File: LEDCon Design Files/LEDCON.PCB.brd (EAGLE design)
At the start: 81.7 x 51.7 mm, 29 parts

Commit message: LEDCON.PCB.v1.0
Everything done. Release version.
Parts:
- U$5: device KW2:RGBLED -> KW2:PLCC4_SMALL
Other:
- board text added: "R.S 2/20/15"
- board text removed: "R.S 2/19/15"
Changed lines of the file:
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@@
 <setting verticaltext="up"/>
 </settings>
-<grid distance="0.1" unitdist="mm" unit="mm" style="lines" multiple="1" display="yes" altdistance="0.000000123031" altunitdist="inch" altunit="inch"/>
+<grid distance="0.0999999999" unitdist="mm" unit="mm" style="lines" multiple="1" display="yes" altdistance="0.000000123031" altunitdist="inch" altunit="inch"/>
 <layers>
 <layer number="1" name="Top" color="4" fill="1" visible="yes" active="yes"/>
@@
 <rectangle x1="2.136709375" y1="19.902615625" x2="2.741228125" y2="19.920396875" layer="21" rot="R180"/>
 <rectangle x1="2.243390625" y1="19.920396875" x2="2.598990625" y2="19.938171875" layer="21" rot="R180"/>
-<text x="-16.26518125" y="20.362359375" size="1.016" layer="21" font="vector" ratio="15" rot="SR0">R.S 2/19/15</text>
+<text x="-16.26518125" y="20.362359375" size="1.016" layer="21" font="vector" ratio="15" rot="SR0">R.S 2/20/15</text>
 </plain>
 <attributes>
@@
 <param name="mdDrill" value="0.25mm"/>
 <param name="mdSmdStop" value="0mil"/>
-<param name="msWidth" value="10mil"/>
-<param name="msDrill" value="24mil"/>
+<param name="msWidth" value="2.75mil"/>
+<param name="msDrill" value="6mil"/>
 <param name="msMicroVia" value="9.99mm"/>
 <param name="msBlindViaRatio" value="0.5"/>
@@
 <param name="rvMicroViaOuter" value="0.25"/>
 <param name="rvMicroViaInner" value="0.25"/>
-<param name="rlMinPadTop" value="1mil"/>
+<param name="rlMinPadTop" value="6mil"/>
 <param name="rlMaxPadTop" value="20mil"/>
 <param name="rlMinPadInner" value="10mil"/>
 <param name="rlMaxPadInner" value="20mil"/>
-<param name="rlMinPadBottom" value="2mil"/>
+<param name="rlMinPadBottom" value="6mil"/>
 <param name="rlMaxPadBottom" value="20mil"/>
 <param name="rlMinViaOuter" value="8mil"/>
@@
 </autorouter>
 <elements>
-<element name="U$1" library="KW2" package="MATE-N-LOK_643230-1" value="" x="3.9116" y="-14.1224" locked="yes" rot="MR180">
+<element name="U$1" library="KW2" package="MATE-N-LOK_643230-1" value="" x="3.9116" y="-14.1224" locked="yes" smashed="yes" rot="MR180">
 <attribute name="MFGN" value="TE Connectivity" x="3.9116" y="-14.1224" size="1.778" layer="28" rot="MR180" display="off"/>
 <attribute name="MFGP" value="643230-1" x="3.9116" y="-14.1224" size="1.778" layer="28" rot="MR180" display="off"/>
+<attribute name="NAME" x="11.9916" y="-10.4724" size="1.27" layer="22" rot="MR180"/>
 </element>
 <element name="U$2" library="GW-devices" package="ESWITCH-TL3301PF" value="" x="-35" y="0" locked="yes" smashed="yes" rot="R90">
@@
 <attribute name="MFGN" value="CUI" x="31.75" y="16.3322" size="1.778" layer="28" rot="MR90" display="off"/>
 <attribute name="MFGP" value="PJ-002A" x="31.75" y="16.3322" size="1.778" layer="28" rot="MR90" display="off"/>
-<attribute name="NAME" x="26.37" y="17.8478" size="1.27" layer="22" rot="MR270"/>
+<attribute name="NAME" x="26.37" y="17.8478" size="1.016" layer="22" rot="MR270"/>
 </element>
 <element name="U$4" library="KW2" package="DF12_F" value="" x="-23.57" y="10" locked="yes" smashed="yes" rot="MR270">
 <attribute name="MFGN" value="Hirose" x="-23.57" y="10" size="1.778" layer="28" rot="MR270" display="off"/>
 <attribute name="MFGP" value="DF12(3.0)-40DP-0.5V(86)" x="-23.57" y="10" size="1.778" layer="28" rot="MR270" display="off"/>
-<attribute name="NAME" x="-28.55" y="11.94" size="1.27" layer="22" rot="MR270"/>
+<attribute name="NAME" x="-28.55" y="11.94" size="1.016" layer="22" rot="MR270"/>
 </element>
 <element name="U$6" library="texas" package="PW_R-PDSO-G14" value="" x="1.4026" y="3.5886" smashed="yes" rot="R270">
@@
 <attribute name="MFGN" value="WorldSemi" x="19.71" y="-2.4" size="1.778" layer="28" rot="MR90" display="off"/>
 <attribute name="MFGP" value="WS2801" x="19.71" y="-2.4" size="1.778" layer="28" rot="MR90" display="off"/>
-<attribute name="NAME" x="18.405" y="-7.58" size="1.27" layer="22" rot="MR180"/>
+<attribute name="NAME" x="18.905" y="-7.58" size="1.016" layer="22" rot="MR180"/>
 <attribute name="VALUE" x="19.075" y="-6.21" size="1.27" layer="28" rot="MR90"/>
 </element>
@@
 <attribute name="MFGN" value="Vishay Dale" x="12.32" y="1.14" size="1.778" layer="28" rot="MR0" display="off"/>
 <attribute name="MFGP" value="CRCW080524R0FKEA" x="12.32" y="1.14" size="1.778" layer="28" rot="MR0" display="off"/>
-<attribute name="NAME" x="10.22" y="0.64" size="1.27" layer="22" rot="MR0"/>
+<attribute name="NAME" x="9.92" y="0.54" size="1.016" layer="22" rot="MR0"/>
 </element>
 <element name="U$16" library="GW-devices" package="RF-C0805" value="24Ohm" x="12.31" y="-1.4" smashed="yes" rot="MR0">
-<attribute name="NAME" x="9.91" y="-2" size="1.27" layer="22" rot="MR0"/>
+<attribute name="NAME" x="9.91" y="-1.8" size="1.016" layer="22" rot="MR0"/>
 <attribute name="MFGN" value="Vishay Dale" x="12.31" y="-1.4" size="1.778" layer="28" rot="MR0" display="off"/>
 <attribute name="MFGP" value="CRCW080524R0FKEA" x="12.31" y="-1.4" size="1.778" layer="28" rot="MR0" display="off"/>
 </element>
 <element name="U$17" library="GW-devices" package="RF-C0805" value="24Ohm" x="12.31" y="-3.64" smashed="yes" rot="MR0">
-<attribute name="NAME" x="9.81" y="-4.34" size="1.27" layer="22" rot="MR0"/>
+<attribute name="NAME" x="10.01" y="-4.14" size="1.016" layer="22" rot="MR0"/>
 <attribute name="MFGN" value="Vishay Dale" x="12.31" y="-3.64" size="1.778" layer="28" rot="MR0" display="off"/>
 <attribute name="MFGP" value="CRCW080524R0FKEA" x="12.31" y="-3.64" size="1.778" layer="28" rot="MR0" display="off"/>
@@
 <attribute name="MFGN" value="CNC Tech" x="-0.635" y="-8.225" size="1.778" layer="28" rot="MR0" display="off"/>
 <attribute name="MFGP" value="3220-20-0100-00" x="-0.635" y="-8.225" size="1.778" layer="28" rot="MR0" display="off"/>
-<attribute name="NAME" x="0.975" y="-13.305" size="1.27" layer="22" rot="MR0"/>
+<attribute name="NAME" x="1.875" y="-12.805" size="1.016" layer="22" rot="MR0"/>
 </element>
 <element name="U$20" library="GW-devices" package="RF-C0805" value="68k" x="11" y="-0.6" smashed="yes" rot="R270">
 <attribute name="MFGN" value="Vishay Dale" x="11" y="-0.6" size="1.778" layer="27" rot="R270" display="off"/>
 <attribute name="MFGP" value="CRCW080568K0FKEA" x="11" y="-0.6" size="1.778" layer="27" rot="R270" display="off"/>
-<attribute name="NAME" x="8.3" y="1.2" size="1.016" layer="21" rot="R270"/>
+<attribute name="NAME" x="8.3" y="0.8" size="1.016" layer="21" rot="R270"/>
 </element>
 <element name="U$21" library="GW-devices" package="RF-C0805" value="68k" x="10.1" y="3.7" smashed="yes" rot="R90">
-<attribute name="NAME" x="7.5" y="5.8" size="1.016" layer="21" rot="R270"/>
+<attribute name="NAME" x="7.8" y="5.5" size="1.016" layer="21" rot="R270"/>
 <attribute name="MFGN" value="Vishay Dale" x="10.1" y="3.7" size="1.778" layer="27" rot="R90" display="off"/>
 <attribute name="MFGP" value="CRCW080568K0FKEA" x="10.1" y="3.7" size="1.778" layer="27" rot="R90" display="off"/>
@@
 <attribute name="MFGN" value="Vishay Dale" x="-21.8" y="-6.6" size="1.778" layer="28" rot="MR180" display="off"/>
 <attribute name="MFGP" value="CRCW080510K0FKEA" x="-21.8" y="-6.6" size="1.778" layer="28" rot="MR180" display="off"/>
-<attribute name="NAME" x="-23.3" y="-8.4" size="1.27" layer="22" rot="MR180"/>
+<attribute name="NAME" x="-23" y="-8.3" size="1.016" layer="22" rot="MR180"/>
 </element>
 <element name="U$10" library="GW-devices" package="C0805" value="0.1uF" x="27" y="13.1" smashed="yes">
@@
 <attribute name="MFGN" value="OnSemi" x="-18" y="-12.3" size="1.778" layer="27" rot="R180" display="off"/>
 <attribute name="MFGP" value="NCP1117ST33T3G" x="-18" y="-12.3" size="1.778" layer="27" rot="R180" display="off"/>
-<attribute name="NAME" x="-14.0932" y="-10.498" size="1.016" layer="21" rot="R270"/>
+<attribute name="NAME" x="-14.0932" y="-11.298" size="1.016" layer="21" rot="R270"/>
 <attribute name="VALUE" x="-22.8768" y="-8.998" size="1.27" layer="27" rot="R270"/>
 </element>
@@
 <attribute name="NAME" x="-18.83" y="-5.77" size="1.016" layer="21" rot="R180"/>
 </element>
-<element name="U$5" library="KW2" package="RGBLED" value="" x="35" y="0" smashed="yes">
+<element name="U$5" library="KW2" package="PLCC4_SMALL" value="" x="35" y="0" smashed="yes">
 <attribute name="MFGN" value="Cree, Inc." x="35" y="0" size="1.778" layer="27" display="off"/>
 <attribute name="MFGP" value="CLV1A-FKB-CK1N1G1BB7R4S3" x="35" y="0" size="1.778" layer="27" display="off"/>
@@
 </signal>
 </signals>
-<errors>
-</errors>
 </board>
 </drawing>

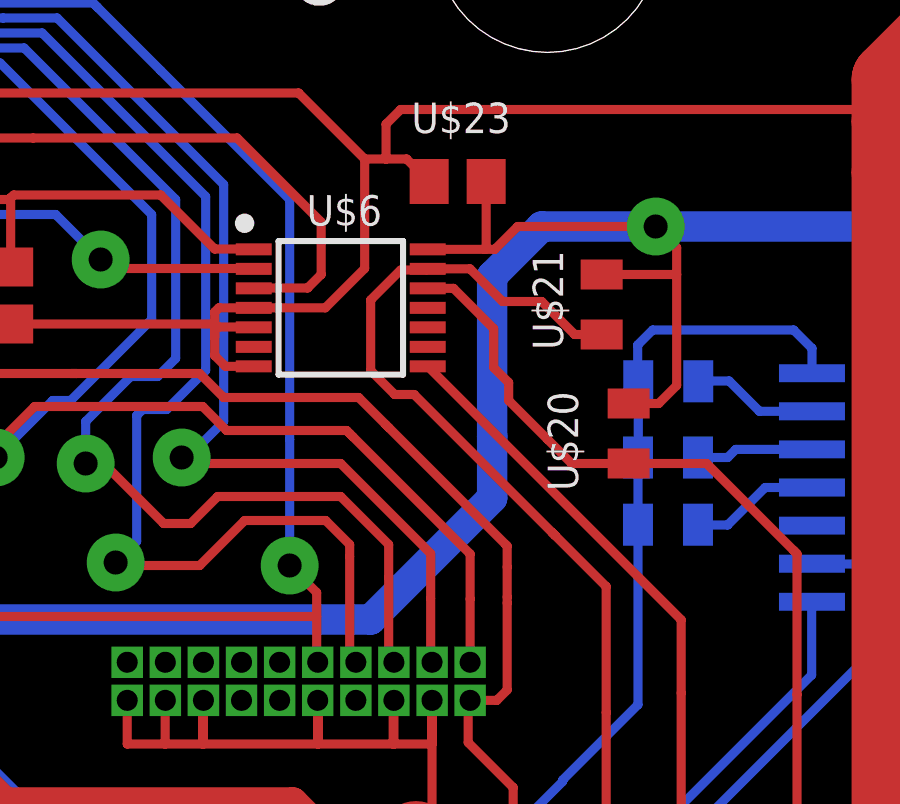
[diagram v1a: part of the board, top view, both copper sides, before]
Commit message: Removed level shifter (no layout change)
Also test commit for branch.
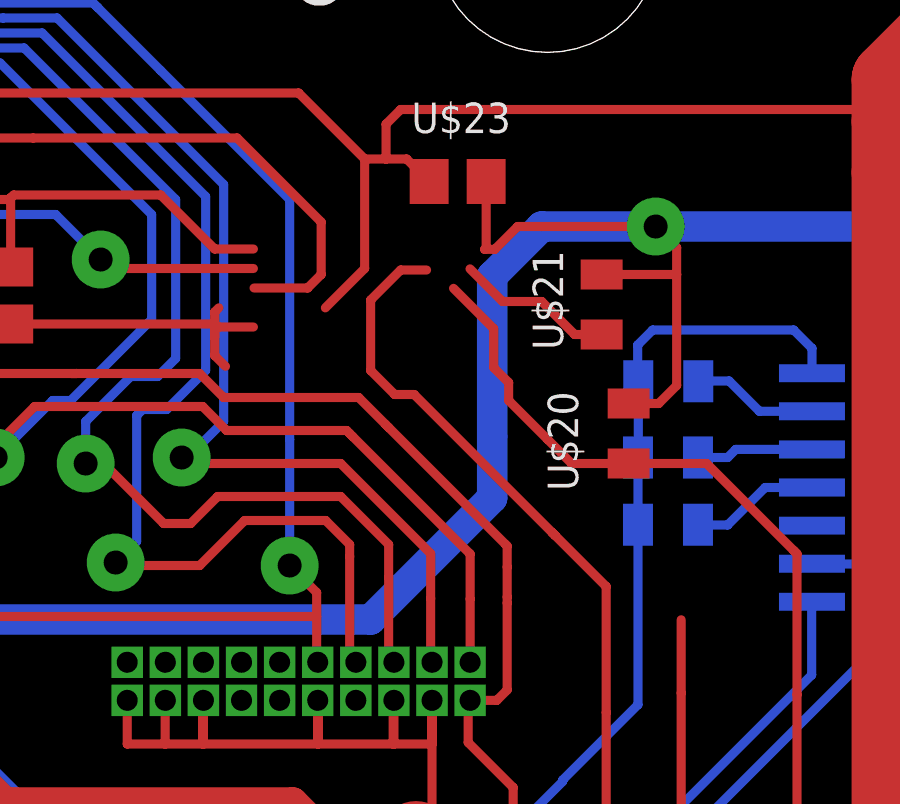
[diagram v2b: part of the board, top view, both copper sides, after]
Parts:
- removed U$6: (no value), texas:PW_R-PDSO-G14
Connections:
- net +3V3: no longer U$6.1, U$6.8
- net CLK_5V: no longer U$6.12
- net DAT_5V: no longer U$6.13
- net GND: no longer U$6.4, U$6.5, U$6.7
- net N$1: no longer U$6.2
- net N$2: no longer U$6.3
- net V+: no longer U$6.14
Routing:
- net +3V3: track 234.5 -> 222.4 mm
- net GND: track 326.4 -> 321.9 mm
- net V+: track 179.3 -> 177.4 mm
- net DAT_5V: track 30.8 -> 29.3 mm
- net CLK_5V: track 26.7 -> 25.9 mm
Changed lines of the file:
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@@
 <?xml version="1.0" encoding="utf-8"?>
 <!DOCTYPE eagle SYSTEM "eagle.dtd">
-<eagle version="6.5.0">
+<eagle version="6.6.0">
 <drawing>
 <settings>
@@
 <attribute name="NAME" x="-28.55" y="11.94" size="1.016" layer="22" rot="MR270"/>
 </element>
-<element name="U$6" library="texas" package="PW_R-PDSO-G14" value="" x="1.4026" y="3.5886" smashed="yes" rot="R270">
-<attribute name="MFGN" value="Texas Instruments" x="1.4026" y="3.5886" size="1.778" layer="27" rot="R270" display="off"/>
-<attribute name="MFGP" value="TXB0104PWR" x="1.4026" y="3.5886" size="1.778" layer="27" rot="R270" display="off"/>
-<attribute name="NAME" x="0.2626" y="6.3286" size="1.016" layer="21"/>
-<attribute name="VALUE" x="-1.1374" y="-0.2214" size="1.27" layer="27"/>
-</element>
 <element name="U$8" library="GW-devices" package="SO14" value="" x="19.71" y="-2.4" smashed="yes" rot="MR90">
 <attribute name="MFGN" value="WorldSemi" x="19.71" y="-2.4" size="1.778" layer="28" rot="MR90" display="off"/>
@@
 <contactref element="U$3" pad="P$2"/>
 <contactref element="U$1" pad="P$1"/>
-<contactref element="U$6" pad="7"/>
-<contactref element="U$6" pad="5"/>
-<contactref element="U$6" pad="4"/>
 <contactref element="U$2" pad="1"/>
 <contactref element="U$2" pad="2"/>
@@
 <wire x1="-21.25" y1="17.25" x2="-21.25" y2="17.1" width="0.3048" layer="16"/>
 <wire x1="-21.25" y1="17.1" x2="-21.25" y2="14.7698" width="0.3048" layer="16"/>
-<wire x1="-1.4974" y1="1.6386" x2="-2.4386" y2="1.6386" width="0.3048" layer="1"/>
 <wire x1="-2.4386" y1="1.6386" x2="-2.8" y2="2" width="0.3048" layer="1"/>
 <wire x1="-2.8" y1="2" x2="-2.8" y2="2.6" width="0.3048" layer="1"/>
 <wire x1="-2.8" y1="2.6" x2="-2.8" y2="2.8" width="0.3048" layer="1"/>
 <wire x1="-2.65" y1="2.95" x2="-1.5088" y2="2.95" width="0.3048" layer="1"/>
-<wire x1="-1.5088" y1="2.95" x2="-1.4974" y2="2.9386" width="0.3048" layer="1"/>
-<wire x1="-1.4974" y1="3.5886" x2="-2.6614" y2="3.5886" width="0.3048" layer="1"/>
 <wire x1="-2.6614" y1="3.5886" x2="-2.8" y2="3.45" width="0.3048" layer="1"/>
 <wire x1="-2.8" y1="3.45" x2="-2.8" y2="3" width="0.3048" layer="1"/>
@@
 <via x="-17.7" y="17.1" extent="1-16" drill="0.8" diameter="1.9304"/>
 <wire x1="-17.7" y1="17.1" x2="-21.25" y2="17.1" width="0.3048" layer="16"/>
-<wire x1="-1.4974" y1="3.5886" x2="0.8886" y2="3.5886" width="0.3048" layer="1"/>
 <wire x1="0.8886" y1="3.5886" x2="2.2" y2="4.9" width="0.3048" layer="1"/>
 <wire x1="2.2" y1="4.9" x2="2.2" y2="8.55" width="0.3048" layer="1"/>
@@
 <wire x1="-34.3" y1="-22.9" x2="-35.3208" y2="-22.9" width="0.3048" layer="16"/>
 <wire x1="-35.3208" y1="-22.9" x2="-35.3208" y2="-22.9108" width="0.3048" layer="16"/>
+<wire x1="-1.5088" y1="2.95" x2="0.8886" y2="3.5886" width="0" layer="19" extent="1-1"/>
 </signal>
 <signal name="+3V3">
 <contactref element="U$4" pad="P$37"/>
-<contactref element="U$6" pad="1"/>
-<contactref element="U$6" pad="8"/>
 <contactref element="U$19" pad="P$1"/>
 <wire x1="12.75" y1="-9.25" x2="12.75" y2="-15.25" width="0.3048" layer="1"/>
@@
 <wire x1="5.65" y1="-10.9" x2="5.65" y2="-9.56" width="0.3048" layer="1"/>
 <wire x1="5.65" y1="-9.56" x2="5.715" y2="-9.495" width="0.3048" layer="1"/>
-<wire x1="4.3412" y1="1.6" x2="4.3026" y2="1.6386" width="0.3048" layer="1"/>
 <via x="-19.35" y="2.4" extent="1-16" drill="0.8" diameter="1.9304"/>
 <via x="14.85" y="-16.85" extent="1-16" drill="0.8" diameter="1.9304"/>
@@
 <wire x1="-4.6" y1="7.35" x2="-2.8" y2="5.55" width="0.3048" layer="1"/>
 <wire x1="-2.8" y1="5.55" x2="-1.5088" y2="5.55" width="0.3048" layer="1"/>
-<wire x1="-1.5088" y1="5.55" x2="-1.4974" y2="5.5386" width="0.3048" layer="1"/>
 <wire x1="6.95" y1="-6.25" x2="6.95" y2="-6.05" width="0.3048" layer="1"/>
 <wire x1="-3.3" y1="1.4" x2="-7.4" y2="1.4" width="0.3048" layer="1"/>
@@
 <wire x1="-19.75" y1="2" x2="-19.35" y2="2.4" width="1.016" layer="16"/>
 <wire x1="12.75" y1="-9.25" x2="12.75" y2="-6.8088" width="0.3048" layer="1"/>
-<wire x1="12.75" y1="-6.8088" x2="4.3026" y2="1.6386" width="0.3048" layer="1"/>
 <contactref element="U$4" pad="P$39"/>
 <wire x1="6.95" y1="-6.05" x2="6.95" y2="-5.05" width="0.3048" layer="1"/>
@@
 <contactref element="U$3" pad="P$1"/>
 <contactref element="U$1" pad="P$4"/>
-<contactref element="U$6" pad="14"/>
 <wire x1="31.75" y1="16.3322" x2="31.75" y2="16.25" width="2.54" layer="1"/>
 <wire x1="31.75" y1="16.25" x2="31.75" y2="12.998740625" width="2.54" layer="1"/>
@@
 <wire x1="22.95" y1="-14.1108" x2="22.9616" y2="-14.1224" width="0.3048" layer="16"/>
 <via x="11.9" y="6.3" extent="1-16" drill="0.8" diameter="1.9304"/>
-<wire x1="4.3026" y1="5.5386" x2="6.2" y2="5.5386" width="0.3048" layer="1"/>
 <wire x1="31.75" y1="13.5" x2="24.55" y2="6.3" width="1.016" layer="16"/>
 <wire x1="24.55" y1="6.3" x2="11.9" y2="6.3" width="1.016" layer="16"/>
@@
 </signal>
 <signal name="DAT_5V">
-<contactref element="U$6" pad="13"/>
 <contactref element="U$1" pad="P$2"/>
 <wire x1="8.45" y1="-3.9" x2="8.55" y2="-4" width="0.3048" layer="1"/>
@@
 <wire x1="2.4" y1="3.85" x2="3.4" y2="4.85" width="0.3048" layer="1"/>
 <wire x1="3.4" y1="4.85" x2="4.264" y2="4.85" width="0.3048" layer="1"/>
-<wire x1="4.264" y1="4.85" x2="4.3026" y2="4.8886" width="0.3048" layer="1"/>
 <wire x1="8.45" y1="-3.9" x2="8.55" y2="-4" width="0.3048" layer="1"/>
 <contactref element="U$21" pad="1"/>
-<wire x1="4.3026" y1="4.8886" x2="5.7114" y2="4.8886" width="0.3048" layer="1"/>
 <wire x1="5.7114" y1="4.8886" x2="6.8" y2="3.8" width="0.3048" layer="1"/>
 <wire x1="9.2" y1="2.7" x2="10.1" y2="2.7" width="0.3048" layer="1"/>
@@
 <wire x1="6.8" y1="3.8" x2="8.1" y2="3.8" width="0.3048" layer="1"/>
 <wire x1="8.1" y1="3.8" x2="9.2" y2="2.7" width="0.3048" layer="1"/>
+<wire x1="4.264" y1="4.85" x2="5.7114" y2="4.8886" width="0" layer="19" extent="1-1"/>
 </signal>
 <signal name="CLK_5V">
 <contactref element="U$1" pad="P$3"/>
-<contactref element="U$6" pad="12"/>
 <wire x1="16.6116" y1="-14.1224" x2="16.6116" y2="-9.3" width="0.3048" layer="1"/>
 <contactref element="U$20" pad="2"/>
-<wire x1="4.3026" y1="4.2386" x2="5.1614" y2="4.2386" width="0.3048" layer="1"/>
 <wire x1="5.1614" y1="4.2386" x2="6.5" y2="2.9" width="0.3048" layer="1"/>
 <wire x1="6.5" y1="2.9" x2="6.5" y2="1.6" width="0.3048" layer="1"/>
@@
 </signal>
 <signal name="N$1">
-<contactref element="U$6" pad="2"/>
 <contactref element="U$4" pad="P$26"/>
 <wire x1="-21.27" y1="8.75" x2="-19.55" y2="8.75" width="0.3048" layer="16"/>
@@
 <via x="-6.6" y="5.2" extent="1-16" drill="0.8" diameter="1.9304"/>
 <wire x1="-3.65" y1="4.9" x2="-1.5088" y2="4.9" width="0.3048" layer="1"/>
-<wire x1="-1.5088" y1="4.9" x2="-1.4974" y2="4.8886" width="0.3048" layer="1"/>
 <wire x1="-3.65" y1="4.9" x2="-5.8" y2="4.9" width="0.3048" layer="1"/>
 <wire x1="-5.8" y1="4.9" x2="-6.3" y2="4.9" width="0.3048" layer="1"/>
@@
 </signal>
 <signal name="N$2">
-<contactref element="U$6" pad="3"/>
 <contactref element="U$4" pad="P$24"/>
 <wire x1="-21.27" y1="9.25" x2="-12" y2="9.25" width="0.3048" layer="16"/>
 <via x="-12" y="9.25" extent="1-16" drill="0.8" diameter="1.9304"/>
 <wire x1="-12" y1="9.25" x2="-8.85" y2="9.25" width="0.3048" layer="1"/>
-<wire x1="-1.5088" y1="4.25" x2="-1.4974" y2="4.2386" width="0.3048" layer="1"/>
 <wire x1="-8.85" y1="9.25" x2="-2.05" y2="9.25" width="0.3048" layer="1"/>
 <wire x1="-2.05" y1="9.25" x2="0.75" y2="6.45" width="0.3048" layer="1"/>
@@
 <wire x1="0.75" y1="4.7" x2="0.3" y2="4.25" width="0.3048" layer="1"/>
 <wire x1="0.3" y1="4.25" x2="-1.486" y2="4.25" width="0.3048" layer="1"/>
-<wire x1="-1.486" y1="4.25" x2="-1.4974" y2="4.2386" width="0.3048" layer="1"/>
 </signal>
 <signal name="N$4">

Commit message: 24V V1
LED still there (need to blast off). Added 24V reg + capacitors
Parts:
- removed U$12: 10uF, GW-devices:C0805
- removed U$20, U$21: 68k, GW-devices:RF-C0805
- removed U$22, U$23: 0.1uF, GW-devices:C0805
- added U$6: 10uF, GW-devices:C1210K
- IC1: device KW2:SOT223 -> SparkFun:TO220-TRACO
- U$13: device GW-devices:C0805 -> GW-devices:C1210K
- moved U$24 9.39 mm to (-20.7, -14.9)
- moved IC1 6.08 mm to (-15.4, -17.8), flipped to the bottom, turned to 270 degrees
- moved U$13 2.93 mm to (-17.1, -6.90), turned to 0 degrees
- moved U$11 1.66 mm to (24.5, 9.20)
- moved U$10 0.28 mm to (26.8, 12.9)
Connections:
- removed net N$1: U$4.P$26
- removed net N$2: U$4.P$24
- net +3V3: now also IC1.OUT, U$5.P$2, U$8.14; no longer IC1.2, IC1.4, U$22.1
- net CLK_5V: now also U$4.P$24; no longer U$20.2
- net DAT_5V: now also U$4.P$26; no longer U$21.1
- net GND: now also IC1.GND, U$6.1; no longer IC1.1, U$12.1, U$22.2, U$23.2
- net V+: now also IC1.IN, U$6.2; no longer IC1.3, U$12.2, U$20.1, U$21.2, U$23.1, U$5.P$2, U$8.14
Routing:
- net +3V3: track 222.4 -> 189.1 mm
- net V+: track 177.4 -> 147.4 mm, vias 3 -> 2
- net CLK_5V: track 25.9 -> 53.8 mm, vias 0 -> 1
- net N$2: track 27.4 -> 0.00 mm, vias 1 -> 0
- net N$1: track 21.4 -> 0.00 mm, vias 1 -> 0
- net DAT_5V: track 29.3 -> 46.5 mm, vias 0 -> 1
- net GND: track 321.9 -> 310.5 mm
- net N$3: track 101.7 -> 100.0 mm
- removed copper zone on layer 1, net GND
- removed copper zone on layer 16, net GND
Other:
- board text added: "LEDCON.PCB.v1.0-24V"
- board text added: "R.S 10/21/15"
- board text removed: "LEDCON.PCB.v1.0"
- board text removed: "R.S 2/20/15"
